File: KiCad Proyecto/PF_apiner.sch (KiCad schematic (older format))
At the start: 7 parts, among them J1 OBDII Header, J2 Conn_01x05, U11 AZ1117EH-3.3TRG1

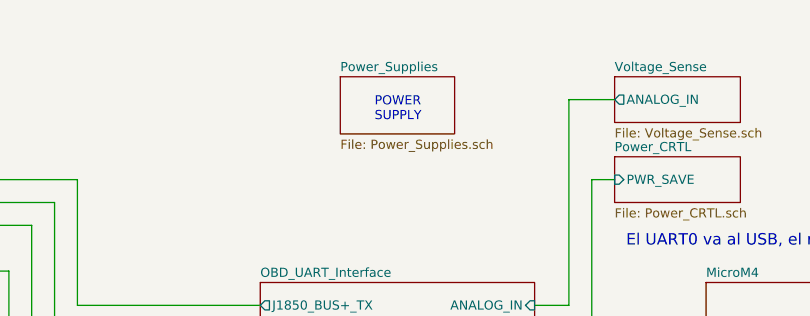
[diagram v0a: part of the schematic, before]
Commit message: added screw holes
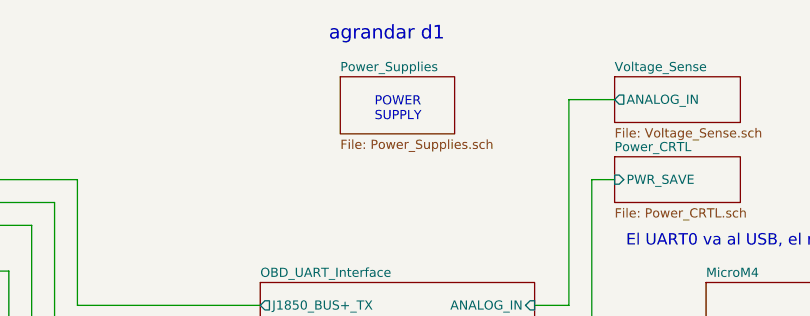
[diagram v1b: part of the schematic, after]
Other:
- note added: "agrandar d1"
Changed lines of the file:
@@
 $EndComp
 Connection ~ 9350 2400
+Text Notes 5400 1350 0    60   ~ 0
+agrandar d1
 $EndSCHEMATC

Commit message: ME curbas PF pos pcb
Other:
- note added: "Revizar footprint Y1 -> osc stn\ngirar footprint 45 grados para que \neste a la misma dist las vias???"
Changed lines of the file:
@@
 Text Notes 5400 1350 0    60   ~ 0
 agrandar d1
+Text Notes 4900 2200 0    60   ~ 0
+Revizar footprint Y1 -> osc stn\ngirar footprint 45 grados para que \neste a la misma dist las vias???
 $EndSCHEMATC

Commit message: modificado pcb
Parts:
- removed C34: 1uF, chip_rlc:c_0402, symbol C
- removed D11: MBR0520, to-sod-sot:SOD-123, symbol D_Schot
- removed U11: AZ1117EH-3.3TRG1, to-sod-sot:SOT-223, symbol VOLT_REG
- added H1, H2, H3, H4: PCB_HOLE, misc:MountingHole_3mm, symbol PCB_HOLE
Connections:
- net labels removed: +3.3V
- wire segments 114 -> 108
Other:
- note removed: "Revizar footprint Y1 -> osc stn\ngirar footprint 45 grados para que \neste a la misma dist las vias???"
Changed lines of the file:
@@
 LIBS:OBDII_IoT
 LIBS:STN2120
-LIBS:PF_apiner-cache
 EELAYER 25 0
 EELAYER END
@@
 $EndComp
 $Comp
-L VOLT_REG U?
-U 1 1 5B8838F5
-P 9550 4350
-AR Path="/582F2211/5B8838F5" Ref="U?"  Part="1"
-AR Path="/5B8838F5" Ref="U11"  Part="1"
-F 0 "U11" H 9400 4600 50  0000 C CNN
-F 1 "AZ1117EH-3.3TRG1" H 9575 4524 40  0000 C CNN
-F 2 "to-sod-sot:SOT-223" H 2000 -850 40  0001 C CNN
-F 3 "" H 2000 -850 40  0000 C CNN
-F 4 "IC REG LDO 3.3V 1A SOT223" H 9550 4350 60  0001 C CNN "Desc"
-F 5 "Diodes Incorporated" H 9550 4350 60  0001 C CNN "Manf"
-F 6 "AZ1117EH-3.3TRG1" H 9550 4350 60  0001 C CNN "Manf#"
-F 7 "AZ1117EH-3.3TRG1DICT-ND" H 9550 4350 60  0001 C CNN "Digikey#"
-	1    9550 4350
-	-1   0    0    -1
-$EndComp
-$Comp
-L C C?
-U 1 1 5B883906
-P 9050 4600
-AR Path="/582F2211/5B883906" Ref="C?"  Part="1"
-AR Path="/5B883906" Ref="C34"  Part="1"
-F 0 "C34" V 8950 4550 50  0000 L CNN
-F 1 "1uF" V 9150 4500 50  0000 L CNN
-F 2 "chip_rlc:c_0402" H 9088 4450 50  0001 C CNN
-F 3 "" H 9050 4600 50  0000 C CNN
-F 4 "CAP CER 1UF 6.3V X5R 0402" H 9050 4600 60  0001 C CNN "Desc"
-F 5 "Taiyo Yuden" H 9050 4600 60  0001 C CNN "Manf"
-F 6 "JMK105BJ105KV-F" H 9050 4600 60  0001 C CNN "Manf#"
-F 7 "587-1231-1-ND" H 9050 4600 60  0001 C CNN "Digikey#"
-	1    9050 4600
-	-1   0    0    -1
-$EndComp
-$Comp
-L +3.3V #PWR?
-U 1 1 5B88390D
-P 8500 4250
-AR Path="/582F2211/5B88390D" Ref="#PWR?"  Part="1"
-AR Path="/5B88390D" Ref="#PWR03"  Part="1"
-F 0 "#PWR03" H 8550 4300 20  0001 C CNN
-F 1 "+3.3V" H 8500 4350 30  0000 C CNN
-F 2 "" H 1750 -450 60  0000 C CNN
-F 3 "" H 1750 -450 60  0000 C CNN
-	1    8500 4250
-	-1   0    0    -1
-$EndComp
-$Comp
-L GND #PWR?
-U 1 1 5B883913
-P 9550 4850
-AR Path="/582F2211/5B883913" Ref="#PWR?"  Part="1"
-AR Path="/5B883913" Ref="#PWR04"  Part="1"
-F 0 "#PWR04" H 9550 4600 50  0001 C CNN
-F 1 "GND" H 9550 4700 50  0001 C CNN
-F 2 "" H 9550 4850 50  0000 C CNN
-F 3 "" H 9550 4850 50  0000 C CNN
-	1    9550 4850
-	-1   0    0    -1
-$EndComp
-$Comp
 L GND #PWR?
 U 1 1 5B883919
 P 10000 4850
 AR Path="/582F2211/5B883919" Ref="#PWR?"  Part="1"
-AR Path="/5B883919" Ref="#PWR05"  Part="1"
-F 0 "#PWR05" H 10000 4600 50  0001 C CNN
+AR Path="/5B883919" Ref="#PWR03"  Part="1"
+F 0 "#PWR03" H 10000 4600 50  0001 C CNN
 F 1 "GND" H 10000 4700 50  0001 C CNN
 F 2 "" H 10000 4850 50  0000 C CNN
@@
 $EndComp
 $Comp
-L GND #PWR?
-U 1 1 5B88391F
-P 9050 4850
-AR Path="/582F2211/5B88391F" Ref="#PWR?"  Part="1"
-AR Path="/5B88391F" Ref="#PWR06"  Part="1"
-F 0 "#PWR06" H 9050 4600 50  0001 C CNN
-F 1 "GND" H 9050 4700 50  0001 C CNN
-F 2 "" H 9050 4850 50  0000 C CNN
-F 3 "" H 9050 4850 50  0000 C CNN
-	1    9050 4850
-	-1   0    0    -1
-$EndComp
-$Comp
-L +5V_USB #U07
+L +5V_USB #U04
 U 1 1 5B88F65F
 P 9250 2300
-F 0 "#U07" H 9250 2450 50  0001 C CNN
+F 0 "#U04" H 9250 2450 50  0001 C CNN
 F 1 "+5V_USB" H 9050 2450 30  0000 L CNN
 F 2 "" H 9250 2300 50  0001 C CNN
@@
 P 10000 4250
 AR Path="/5B89C1C4/5B8A5F5E" Ref="#PWR?"  Part="1"
-AR Path="/5B8A5F5E" Ref="#PWR08"  Part="1"
-F 0 "#PWR08" H 10000 4340 20  0001 C CNN
+AR Path="/5B8A5F5E" Ref="#PWR05"  Part="1"
+F 0 "#PWR05" H 10000 4340 20  0001 C CNN
 F 1 "+5V" H 10000 4340 30  0000 C CNN
 F 2 "" H 10000 4250 60  0000 C CNN
@@
 P 10650 4250
 AR Path="/5B89C1C4/5B8A5F68" Ref="U?"  Part="1"
-AR Path="/5B8A5F68" Ref="#U09"  Part="1"
-F 0 "#U09" H 10650 4400 50  0001 C CNN
+AR Path="/5B8A5F68" Ref="#U06"  Part="1"
+F 0 "#U06" H 10650 4400 50  0001 C CNN
 F 1 "+5V_USB" H 10697 4279 30  0000 L CNN
 F 2 "" H 10650 4250 50  0001 C CNN
@@
 $EndComp
 $Comp
-L D_Schot D?
-U 1 1 5B8B67B7
-P 8850 4350
-AR Path="/5B89C1C4/5B8B67B7" Ref="D?"  Part="1"
-AR Path="/5B8B67B7" Ref="D11"  Part="1"
-F 0 "D11" H 8800 4430 50  0000 L CNN
-F 1 "MBR0520" H 8730 4250 40  0000 L CNN
-F 2 "to-sod-sot:SOD-123" V 8850 4350 50  0001 C CNN
-F 3 "" V 8850 4350 50  0000 C CNN
-F 4 "DIODE SCHOTTKY 20V 500MA SOD123" H 8850 4350 50  0001 C CNN "Desc"
-F 5 "ON Semiconductor" H 8850 4350 50  0001 C CNN "Manf"
-F 6 "MBR0520LT1G" H 8850 4350 50  0001 C CNN "Manf#"
-F 7 "MBR0520LT1GOSCT-ND" H 8850 4350 50  0001 C CNN "Digikey#"
-	1    8850 4350
-	1    0    0    -1
-$EndComp
-$Comp
 L GND #PWR?
 U 1 1 5B8BA0D1
 P 8900 3050
 AR Path="/582F2211/5B8BA0D1" Ref="#PWR?"  Part="1"
-AR Path="/5B8BA0D1" Ref="#PWR010"  Part="1"
-F 0 "#PWR010" H 8900 2800 50  0001 C CNN
+AR Path="/5B8BA0D1" Ref="#PWR07"  Part="1"
+F 0 "#PWR07" H 8900 2800 50  0001 C CNN
 F 1 "GND" H 8900 2900 50  0001 C CNN
 F 2 "" H 8900 3050 50  0000 C CNN
@@
 $EndComp
 $Comp
-L PWR_FLAG #FLG011
+L PWR_FLAG #FLG08
 U 1 1 5BA598FF
 P 9350 2200
-F 0 "#FLG011" H 9350 2295 50  0001 C CNN
+F 0 "#FLG08" H 9350 2295 50  0001 C CNN
 F 1 "PWR_FLAG" H 9350 2380 40  0000 C CNN
 F 2 "" H 9350 2200 50  0000 C CNN
@@
 	10000 4250 10000 4450
 Wire Wire Line
-	9950 4350 10250 4350
-Wire Wire Line
 	10000 4750 10000 4850
-Wire Wire Line
-	9550 4800 9550 4850
-Wire Wire Line
-	9050 4850 9050 4750
-Wire Wire Line
-	8950 4350 9100 4350
 Wire Wire Line
 	9250 2300 9250 2400
@@
 Connection ~ 10000 4350
 Wire Wire Line
-	8500 4250 8500 4350
-Wire Wire Line
-	8500 4350 8750 4350
-Wire Wire Line
 	8900 2900 9350 2900
 Wire Wire Line
@@
 Wire Wire Line
 	9350 2200 9350 2500
-Wire Wire Line
-	9050 4450 9050 4350
-Connection ~ 9050 4350
 $Comp
 L Conn_01x05 J2
@@
 Text Notes 5400 1350 0    60   ~ 0
 agrandar d1
-Text Notes 4900 2200 0    60   ~ 0
-Revizar footprint Y1 -> osc stn\ngirar footprint 45 grados para que \neste a la misma dist las vias???
+Wire Wire Line
+	10000 4350 10250 4350
+$Comp
+L PCB_HOLE H4
+U 1 1 5BDBC2D4
+P 10050 3650
+F 0 "H4" H 9900 3650 60  0000 C CNN
+F 1 "PCB_HOLE" H 10350 3650 60  0000 C CNN
+F 2 "misc:MountingHole_3mm" H 9900 3700 60  0001 C CNN
+F 3 "PCB HOLE" H 10000 3800 60  0001 C CNN
+	1    10050 3650
+	1    0    0    -1
+$EndComp
+$Comp
+L PCB_HOLE H3
+U 1 1 5BDBD6A0
+P 10050 3500
+F 0 "H3" H 9900 3500 60  0000 C CNN
+F 1 "PCB_HOLE" H 10350 3500 60  0000 C CNN
+F 2 "misc:MountingHole_3mm" H 9900 3550 60  0001 C CNN
+F 3 "PCB HOLE" H 10000 3650 60  0001 C CNN
+	1    10050 3500
+	1    0    0    -1
+$EndComp
+$Comp
+L PCB_HOLE H2
+U 1 1 5BDBD82A
+P 10050 3350
+F 0 "H2" H 9900 3350 60  0000 C CNN
+F 1 "PCB_HOLE" H 10350 3350 60  0000 C CNN
+F 2 "misc:MountingHole_3mm" H 9900 3400 60  0001 C CNN
+F 3 "PCB HOLE" H 10000 3500 60  0001 C CNN
+	1    10050 3350
+	1    0    0    -1
+$EndComp
+$Comp
+L PCB_HOLE H1
+U 1 1 5BDBD9BA
+P 10050 3200
+F 0 "H1" H 9900 3200 60  0000 C CNN
+F 1 "PCB_HOLE" H 10350 3200 60  0000 C CNN
+F 2 "misc:MountingHole_3mm" H 9900 3250 60  0001 C CNN
+F 3 "PCB HOLE" H 10000 3350 60  0001 C CNN
+	1    10050 3200
+	1    0    0    -1
+$EndComp
 $EndSCHEMATC
